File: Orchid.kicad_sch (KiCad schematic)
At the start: 122 parts, among them U1 nice_nano, U2 nice_nano

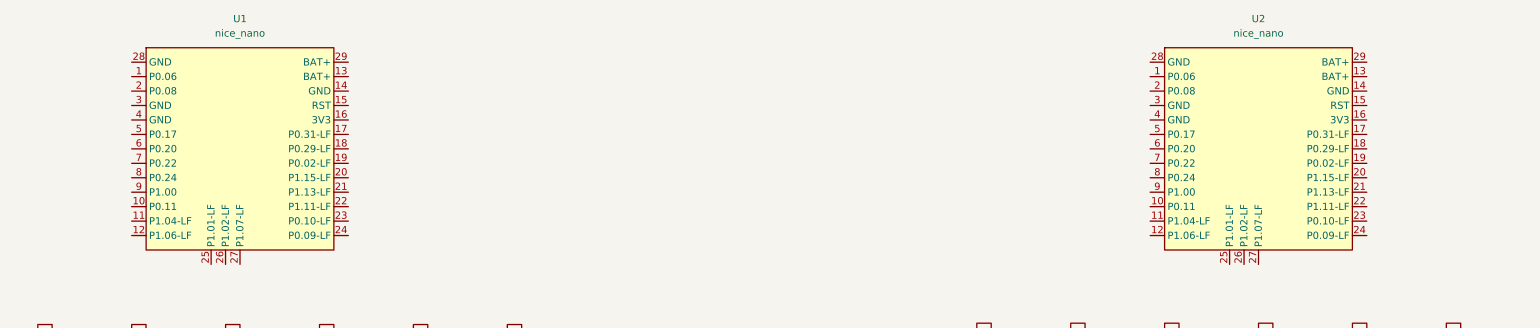
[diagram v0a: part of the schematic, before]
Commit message: Added components.
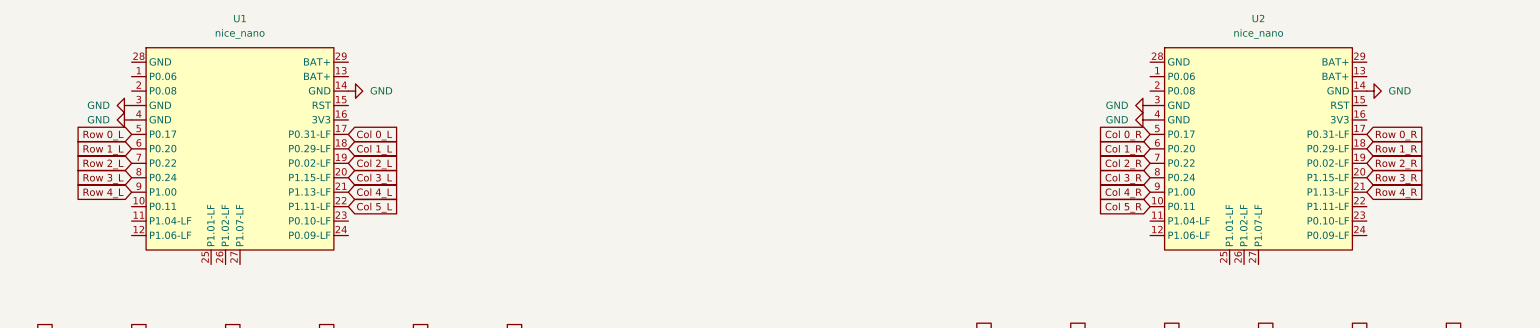
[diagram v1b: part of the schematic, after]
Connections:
- net Col 0_L: now also U1.17 (P0.31-LF)
- net Col 0_R: now also U2.5 (P0.17)
- net Col 1_L: now also U1.18 (P0.29-LF)
- net Col 1_R: now also U2.6 (P0.20)
- net Col 2_L: now also U1.19 (P0.02-LF)
- net Col 2_R: now also U2.7 (P0.22)
- net Col 3_L: now also U1.20 (P1.15-LF)
- net Col 3_R: now also U2.8 (P0.24)
- net Col 4_L: now also U1.21 (P1.13-LF)
- net Col 4_R: now also U2.9 (P1.00)
- net Col 5_L: now also U1.22 (P1.11-LF)
- net Col 5_R: now also U2.10 (P0.11)
- net Row 0_L: now also U1.5 (P0.17)
- net Row 0_R: now also U2.17 (P0.31-LF)
- net Row 1_L: now also U1.6 (P0.20)
- net Row 1_R: now also U2.18 (P0.29-LF)
- net Row 2_L: now also U1.7 (P0.22)
- net Row 2_R: now also U2.19 (P0.02-LF)
- net Row 3_L: now also U1.8 (P0.24)
- net Row 3_R: now also U2.20 (P1.15-LF)
- net Row 4_L: now also U1.9 (P1.00)
- net Row 4_R: now also U2.21 (P1.13-LF)
- net GND: now reaches U2.14 (GND)
- net GND: now also U1.14 (GND), U1.3 (GND), U1.4 (GND), U2.3 (GND), U2.4 (GND)

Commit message: Completed the diagram.
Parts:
- added J1: Battery_L, symbol Connector_Generic:Conn_01x02
- added J2: Battery_R, symbol Connector_Generic:Conn_01x02
- added Reset_L, Reset_R: SW_Push, symbol Switch:SW_Push
- added SW1, SW2: SW_DPDT_x2, symbol Switch:SW_DPDT_x2
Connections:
- net BAT+_R: now reaches U2.13 (BAT+)
- net BAT+_R: now also SW2.2 (B)
- net RESET_R: now reaches U2.15 (RST)
- net RESET_R: now also Reset_R.1
- net BAT+_L: now reaches U1.13 (BAT+)
- net BAT+_L: now also SW1.2 (B)
- net RESET_L: now reaches U1.15 (RST)
- net RESET_L: now also Reset_L.1
- net GND renamed GND_L
- net GND_L: now also J1.2 (Pin_2), J2.2 (Pin_2), Reset_L.2; no longer U2.14 (GND), U2.3 (GND), U2.4 (GND)
- new net: J2.1 (Pin_1), SW2.1 (A)
- new net: J1.1 (Pin_1), SW1.1 (A)
- new net GND_R: Reset_R.2, U2.14 (GND), U2.3 (GND), U2.4 (GND)
- no-connect marks 0 -> 2

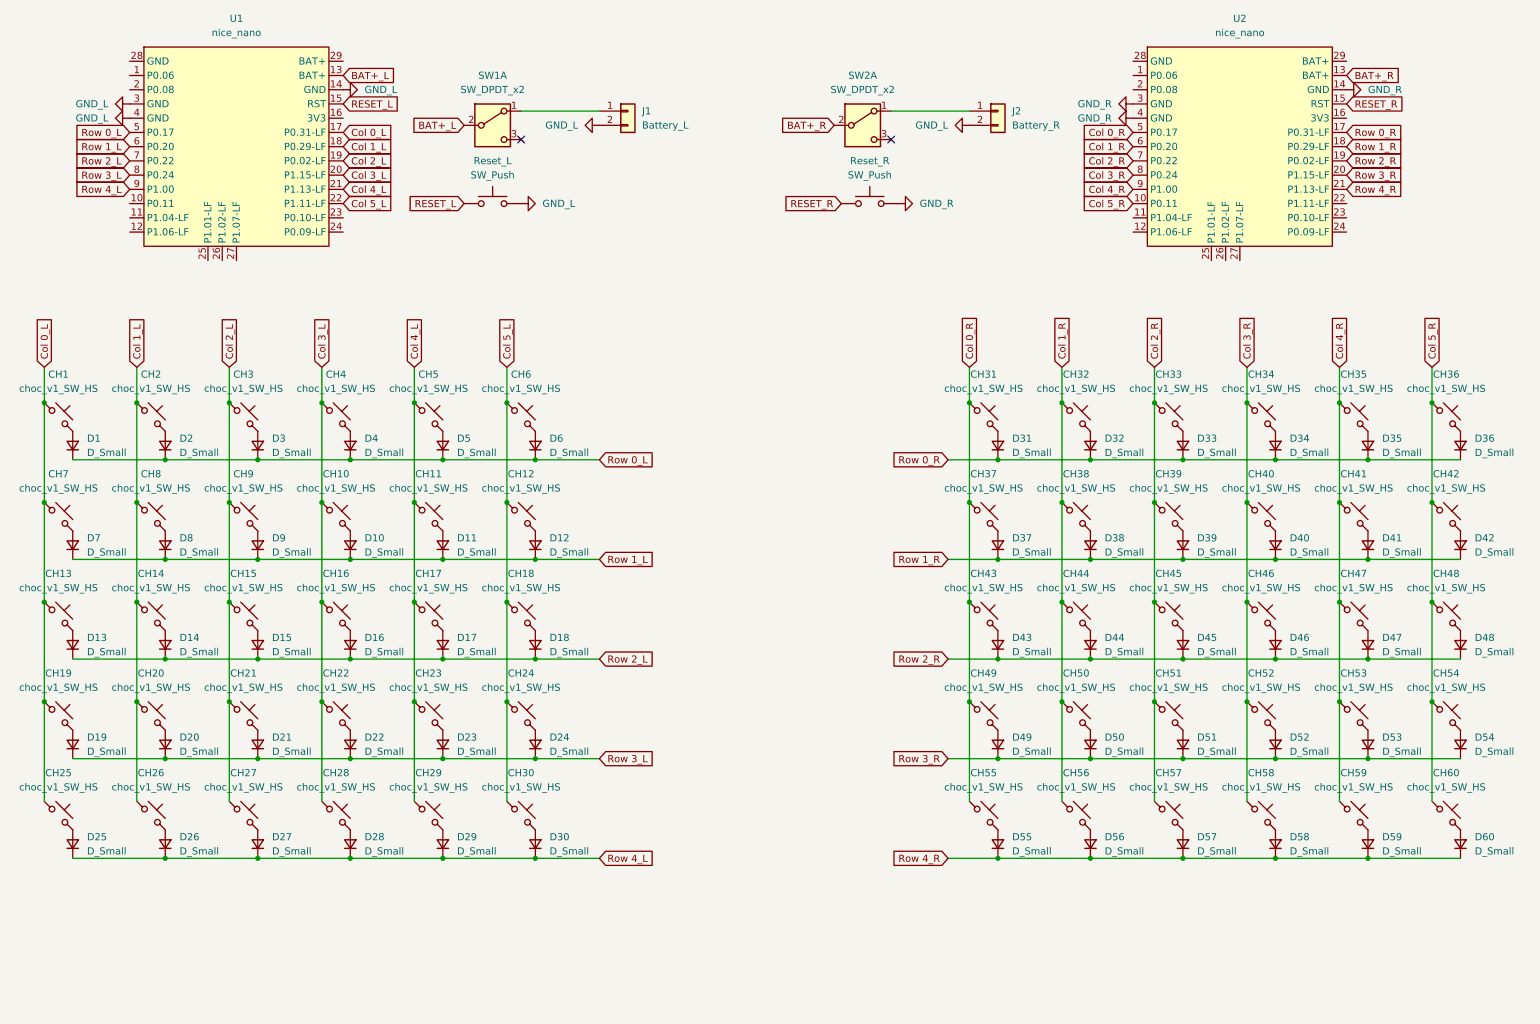
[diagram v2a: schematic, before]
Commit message: Added niceview.
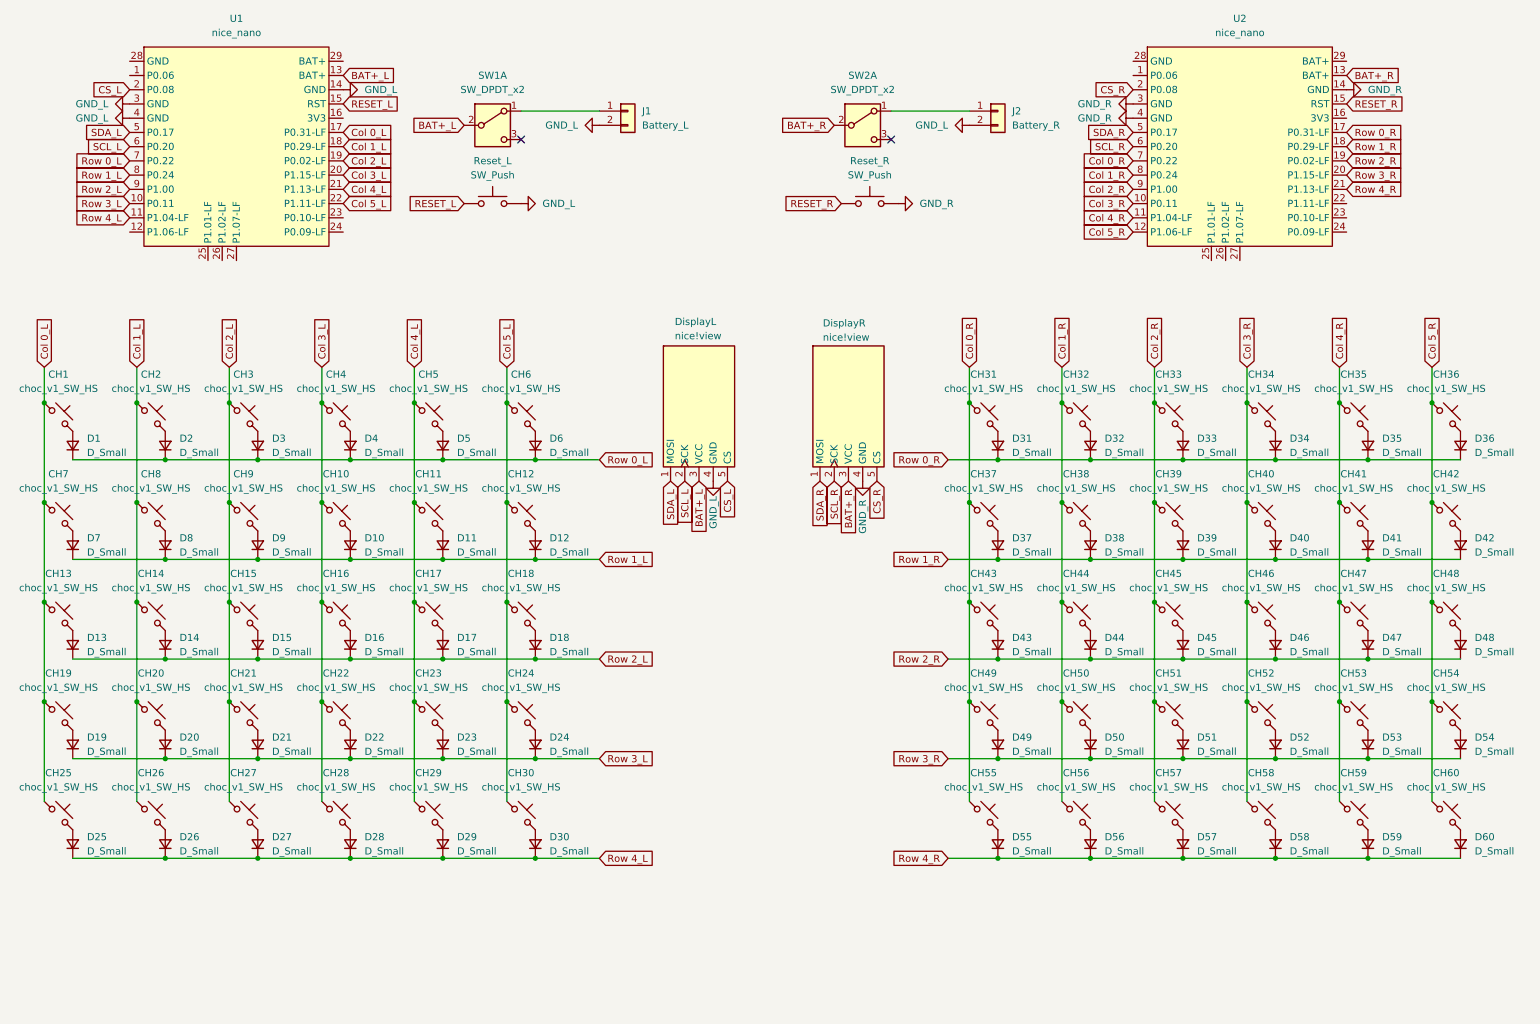
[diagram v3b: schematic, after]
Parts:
- added DisplayL, DisplayR: nice!view, nice_view:nice_view, symbol nice_view:nice!view
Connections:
- net BAT+_L: now also DisplayL.3 (VCC)
- net BAT+_R: now also DisplayR.3 (VCC)
- net Col 0_R: now also U2.7 (P0.22); no longer U2.5 (P0.17)
- net Col 1_R: now also U2.8 (P0.24); no longer U2.6 (P0.20)
- net Col 2_R: now also U2.9 (P1.00); no longer U2.7 (P0.22)
- net Col 3_R: now also U2.10 (P0.11); no longer U2.8 (P0.24)
- net Col 4_R: now also U2.11 (P1.04-LF); no longer U2.9 (P1.00)
- net Col 5_R: now also U2.12 (P1.06-LF); no longer U2.10 (P0.11)
- net GND_L: now also DisplayL.4 (GND)
- net GND_R: now also DisplayR.4 (GND)
- net Row 0_L: now also U1.7 (P0.22); no longer U1.5 (P0.17)
- net Row 1_L: now also U1.8 (P0.24); no longer U1.6 (P0.20)
- net Row 2_L: now also U1.9 (P1.00); no longer U1.7 (P0.22)
- net Row 3_L: now also U1.10 (P0.11); no longer U1.8 (P0.24)
- net Row 4_L: now also U1.11 (P1.04-LF); no longer U1.9 (P1.00)
- net CS_R: now reaches U2.2 (P0.08)
- net CS_R: now also DisplayR.5 (CS)
- net CS_L: now reaches U1.2 (P0.08)
- net CS_L: now also DisplayL.5 (CS)
- new net SCL_L: DisplayL.2 (SCK), U1.6 (P0.20)
- new net SCL_R: DisplayR.2 (SCK), U2.6 (P0.20)
- new net SDA_L: DisplayL.1 (MOSI), U1.5 (P0.17)
- new net SDA_R: DisplayR.1 (MOSI), U2.5 (P0.17)

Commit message: vcc.
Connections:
- net BAT+_L: no longer DisplayL.3 (VCC)
- net BAT+_R: no longer DisplayR.3 (VCC)
- net VCC_R: now reaches U2.16 (3V3)
- net VCC_R: now also DisplayR.3 (VCC)
- net VCC_L: now reaches U1.16 (3V3)
- net VCC_L: now also DisplayL.3 (VCC)

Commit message: Assigned footprints.
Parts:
- D1, D10, D11, D12, D13, D14, D15, D16, D17, D18, D19, D2, D20, D21, D22, D23, D24, D25, D26, D27, D28, D29, D3, D30, D31, D32, D33, D34, D35, D36, D37, D38, D39, D4, D40, D41, D42, D43, D44, D45, D46, D47, D48, D49, D5, D50, D51, D52, D53, D54, D55, D56, D57, D58, D59, D6, D60, D7, D8, D9: footprint (none) -> random-keyboard-parts:D_SOD-123-Pretty
- J1, J2: footprint (none) -> PCM_marbastlib-various:CON_JST_ACH_BM02B
- Reset_L1: renamed from Reset_L; footprint (none) -> random-keyboard-parts:Reset_Pretty
- Reset_R1: renamed from Reset_R; footprint (none) -> random-keyboard-parts:Reset_Pretty
- SW1, SW2: footprint (none) -> PCM_marbastlib-various:SW_SKHLLCA010
- renumbered DisplayL to DisplayL1, DisplayR to DisplayR1

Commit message: Added title.
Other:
- note added: "1 1"
- note added: "Orchid keyboard V1"
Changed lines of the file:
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@@
+		)
+	)
+	(text "1 1"
+		(exclude_from_sim no)
+		(at 186.69 183.642 0)
+		(effects
+			(font
+				(size 1.27 1.27)
+			)
+		)
+	)
+	(text "Orchid keyboard V1\n"
+		(exclude_from_sim no)
+		(at 199.39 189.738 0)
+		(effects
+			(font
+				(size 1.778 1.778)
+				(thickness 0.3556)
+				(bold yes)
+			)
 		)
 	)
